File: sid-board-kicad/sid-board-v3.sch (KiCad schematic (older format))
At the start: 48 parts, among them J1 SPI + UART, J2 USB_B_Micro, Q1 BSS138, Q2 BSS138, SW1 SW_EN, SW2 SW_FLASH, U1 SC16IS752IPW, U2 MCP1703A-3302_SOT223, U3 SN65HVD232, U4 SN65HVD232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

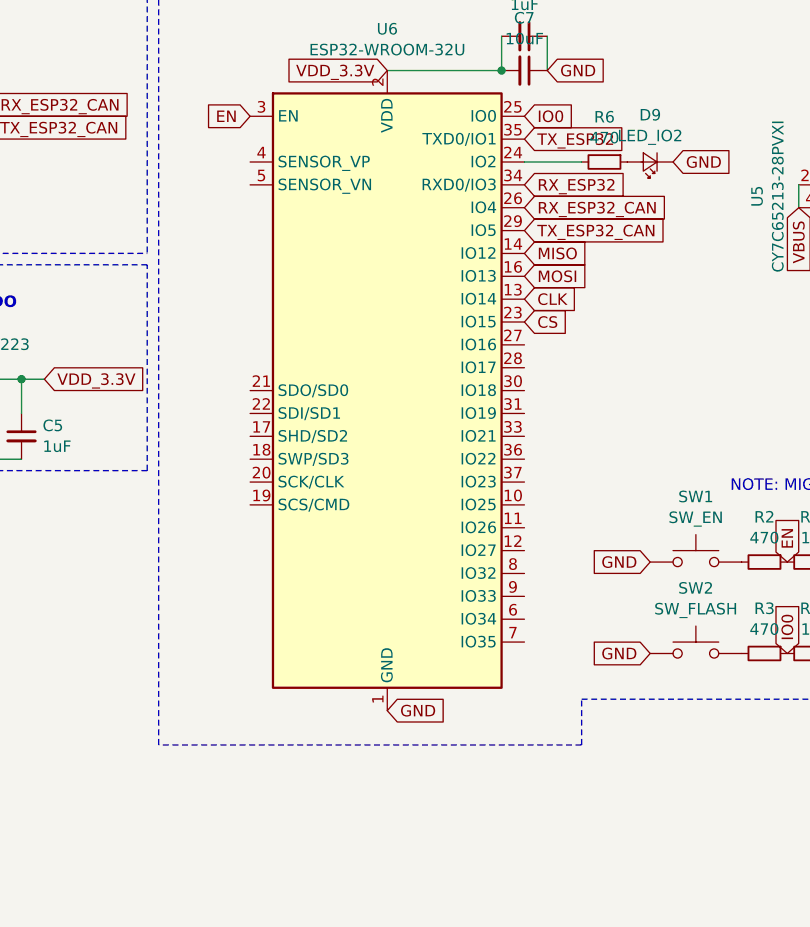
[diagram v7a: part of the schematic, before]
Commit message: Added IO expansion for free pins on ESP32
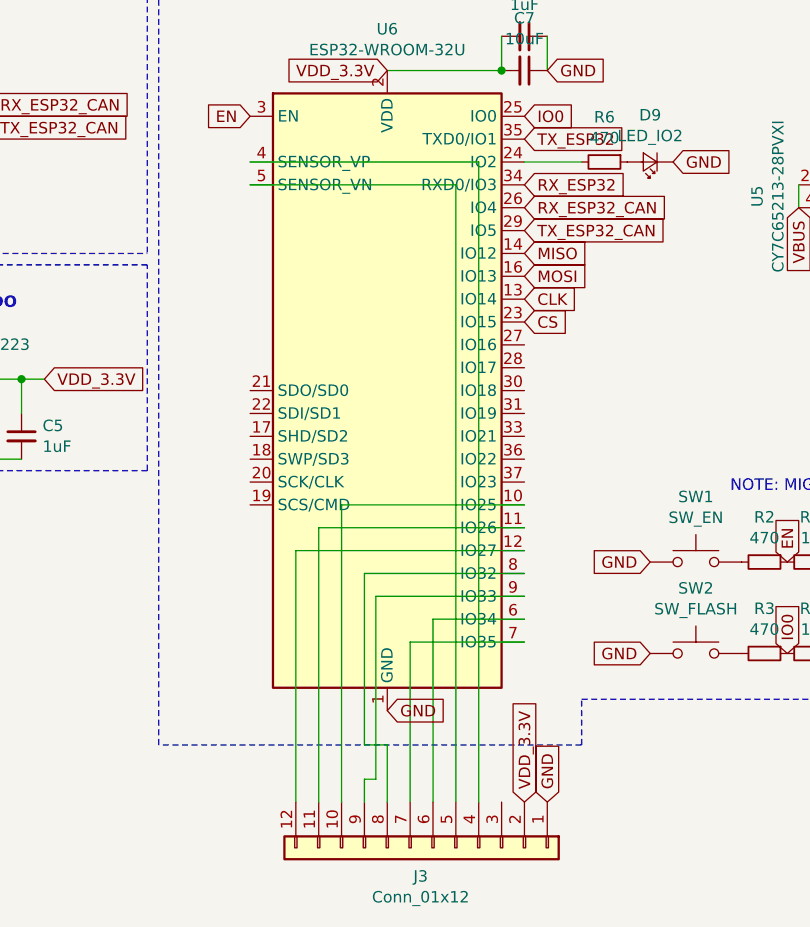
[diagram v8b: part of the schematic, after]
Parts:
- added J3: Conn_01x12, Connector_PinHeader_2.54mm:PinHeader_1x12_P2.54mm_Vertical, symbol Connector_Generic:Conn_01x12
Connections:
- net GND: now also J3.1 (Pin_1)
- net VDD_3.3V: now also J3.2 (Pin_2)
- net at U6.10 (IO25): now also J3.10 (Pin_10)
- net at U6.11 (IO26): now also J3.11 (Pin_11)
- net at U6.12 (IO27): now also J3.12 (Pin_12)
- net at U6.4 (SENSOR_VP): now also J3.4 (Pin_4)
- net at U6.5 (SENSOR_VN): now also J3.5 (Pin_5)
- net at U6.6 (IO34): now also J3.6 (Pin_6)
- net at U6.7 (IO35): now also J3.7 (Pin_7)
- net at U6.8 (IO32): now also J3.8 (Pin_8)
- net at U6.9 (IO33): now also J3.9 (Pin_9)
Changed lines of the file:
@@
 	1    0    0    -1
 $EndComp
+$Comp
+L Connector_Generic:Conn_01x12 J3
+U 1 1 5F374BE1
+P 5500 7050
+F 0 "J3" V 5625 6996 50  0000 C CNN
+F 1 "Conn_01x12" V 5716 6996 50  0000 C CNN
+F 2 "Connector_PinHeader_2.54mm:PinHeader_1x12_P2.54mm_Vertical" H 5500 7050 50  0001 C CNN
+F 3 "~" H 5500 7050 50  0001 C CNN
+	1    5500 7050
+	0    1    1    0
+$EndComp
+Text GLabel 5900 6850 1    50   Input ~ 0
+VDD_3.3V
+Text GLabel 6000 6850 1    50   Input ~ 0
+GND
+Wire Wire Line
+	4700 4050 5700 4050
+Wire Wire Line
+	5700 4050 5700 6850
+Wire Wire Line
+	4700 4150 5600 4150
+Wire Wire Line
+	5600 4150 5600 6850
+Wire Wire Line
+	5900 6050 5500 6050
+Wire Wire Line
+	5500 6050 5500 6850
+Wire Wire Line
+	5900 6150 5400 6150
+Wire Wire Line
+	5400 6150 5400 6850
+Wire Wire Line
+	5900 5850 5200 5850
+Wire Wire Line
+	5200 5850 5200 6600
+Wire Wire Line
+	5200 6600 5300 6600
+Wire Wire Line
+	5300 6600 5300 6850
+Wire Wire Line
+	5900 5950 5250 5950
+Wire Wire Line
+	5250 5950 5250 6750
+Wire Wire Line
+	5250 6750 5200 6750
+Wire Wire Line
+	5200 6750 5200 6850
+Wire Wire Line
+	5900 5550 5100 5550
+Wire Wire Line
+	5100 5550 5100 6850
+Wire Wire Line
+	5900 5650 5000 5650
+Wire Wire Line
+	5000 5650 5000 6850
+Wire Wire Line
+	5900 5750 4900 5750
+Wire Wire Line
+	4900 5750 4900 6850
 $EndSCHEMATC
